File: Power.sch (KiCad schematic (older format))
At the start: 20 parts, among them U11 MCP1825S, U12 MP2456GJ-Z, U13 TLV75533PDBV

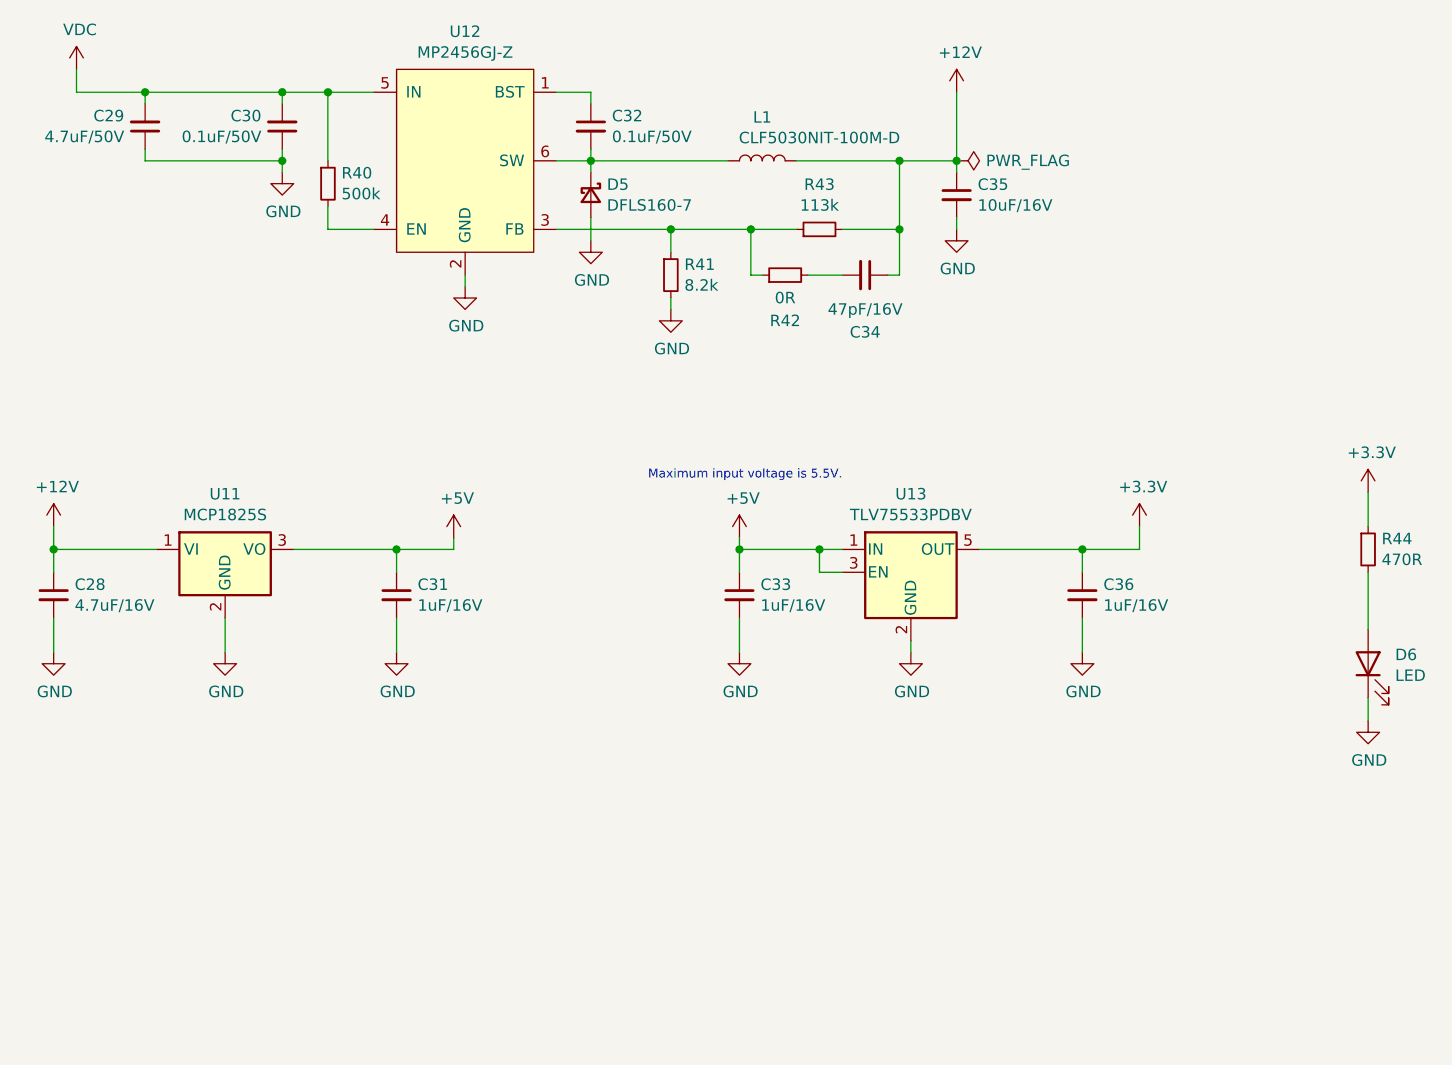
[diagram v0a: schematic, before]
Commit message: Update: 回路図、DCリンクCap1つ削除、アノテーションリセット
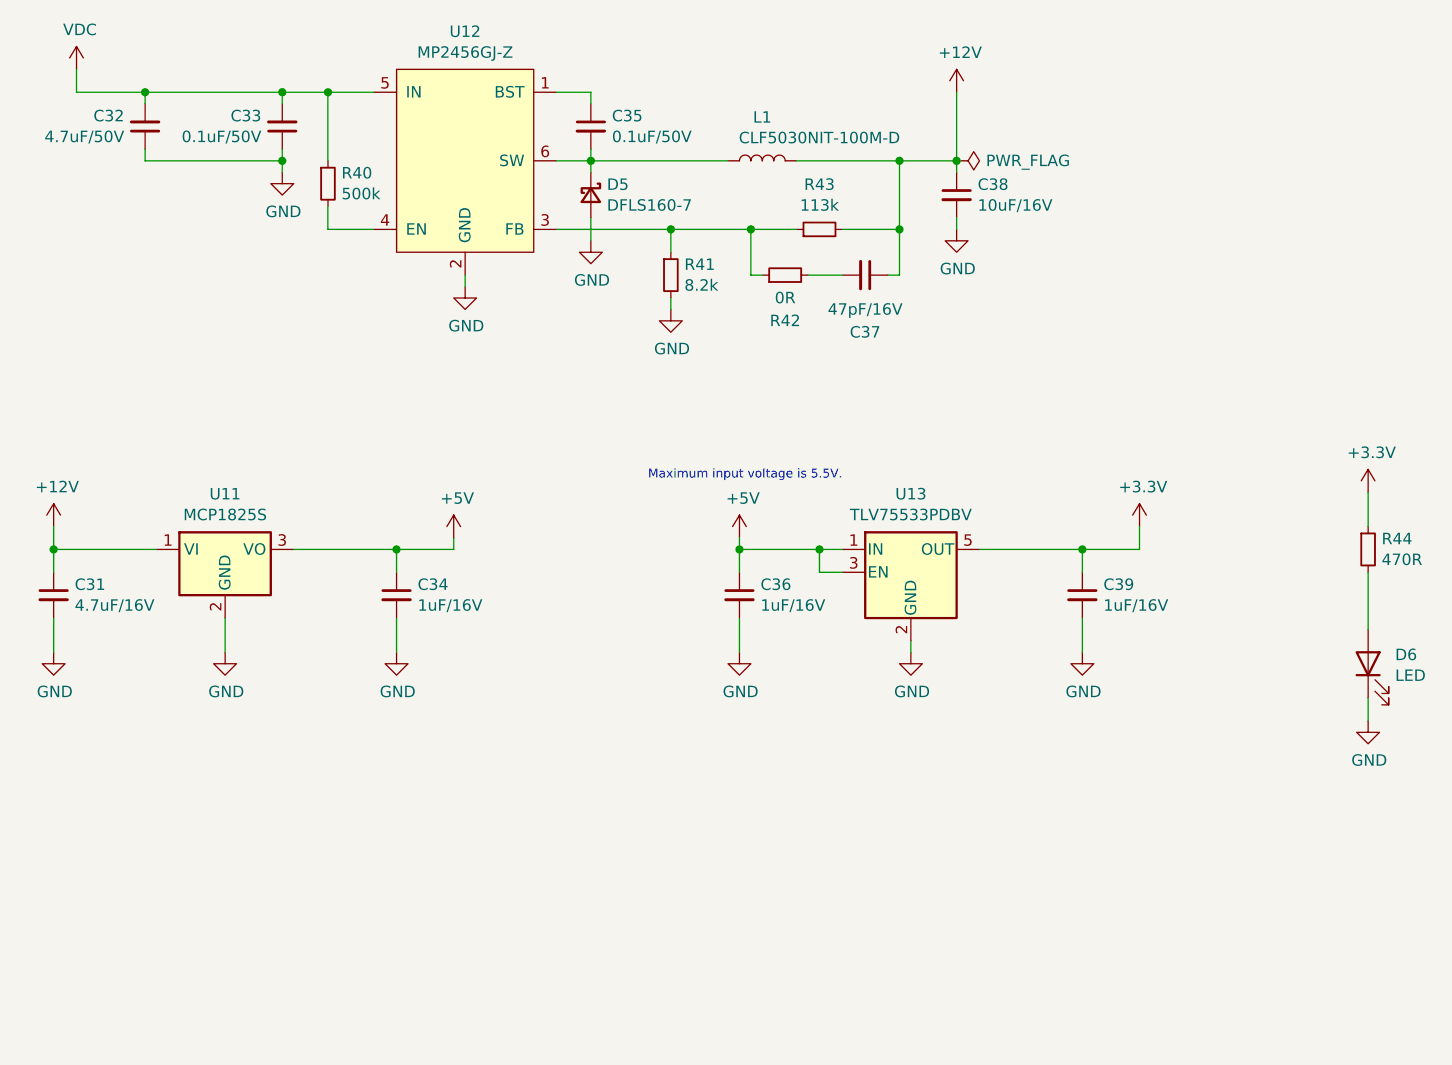
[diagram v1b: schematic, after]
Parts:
- renumbered C28 to C31, C29 to C32, C30 to C33, C31 to C34, C32 to C35, C33 to C36, C34 to C37, C35 to C38, C36 to C39
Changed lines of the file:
@@
 P 6700 1950
 AR Path="/60984E4D" Ref="C?"  Part="1"
-AR Path="/6093BF63/60984E4D" Ref="C35"  Part="1"
-F 0 "C35" H 6792 1996 50  0000 L CNN
+AR Path="/6093BF63/60984E4D" Ref="C38"  Part="1"
+F 0 "C38" H 6792 1996 50  0000 L CNN
 F 1 "10uF/16V" H 6792 1905 50  0000 L CNN
 F 2 "Capacitor_SMD:C_0805_2012Metric" H 6700 1950 50  0001 C CNN
@@
 P 5100 1650
 AR Path="/60984E53" Ref="C?"  Part="1"
-AR Path="/6093BF63/60984E53" Ref="C32"  Part="1"
-F 0 "C32" H 5192 1696 50  0000 L CNN
+AR Path="/6093BF63/60984E53" Ref="C35"  Part="1"
+F 0 "C35" H 5192 1696 50  0000 L CNN
 F 1 "0.1uF/50V" H 5192 1605 50  0000 L CNN
 F 2 "Capacitor_SMD:C_0603_1608Metric" H 5100 1650 50  0001 C CNN
@@
 P 3750 1650
 AR Path="/60984E87" Ref="C?"  Part="1"
-AR Path="/6093BF63/60984E87" Ref="C30"  Part="1"
-F 0 "C30" H 3659 1604 50  0000 R CNN
+AR Path="/6093BF63/60984E87" Ref="C33"  Part="1"
+F 0 "C33" H 3659 1604 50  0000 R CNN
 F 1 "0.1uF/50V" H 3659 1695 50  0000 R CNN
 F 2 "Capacitor_SMD:C_0603_1608Metric" H 3750 1650 50  0001 C CNN
@@
 P 6300 2300
 AR Path="/60984EA5" Ref="C?"  Part="1"
-AR Path="/6093BF63/60984EA5" Ref="C34"  Part="1"
-F 0 "C34" V 6550 2300 50  0000 C CNN
+AR Path="/6093BF63/60984EA5" Ref="C37"  Part="1"
+F 0 "C37" V 6550 2300 50  0000 C CNN
 F 1 "47pF/16V" V 6450 2300 50  0000 C CNN
 F 2 "Capacitor_SMD:C_0603_1608Metric" H 6300 2300 50  0001 C CNN
@@
 P 3150 1650
 AR Path="/60984EB3" Ref="C?"  Part="1"
-AR Path="/6093BF63/60984EB3" Ref="C29"  Part="1"
-F 0 "C29" H 3059 1604 50  0000 R CNN
+AR Path="/6093BF63/60984EB3" Ref="C32"  Part="1"
+F 0 "C32" H 3059 1604 50  0000 R CNN
 F 1 "4.7uF/50V" H 3059 1695 50  0000 R CNN
 F 2 "Capacitor_SMD:C_0805_2012Metric" H 3150 1650 50  0001 C CNN
@@
 P 2750 3700
 AR Path="/633C9961" Ref="C?"  Part="1"
-AR Path="/6093BF63/633C9961" Ref="C28"  Part="1"
-F 0 "C28" H 2842 3746 50  0000 L CNN
+AR Path="/6093BF63/633C9961" Ref="C31"  Part="1"
+F 0 "C31" H 2842 3746 50  0000 L CNN
 F 1 "4.7uF/16V" H 2842 3655 50  0000 L CNN
 F 2 "Capacitor_SMD:C_0805_2012Metric" H 2750 3700 50  0001 C CNN
@@
 P 4250 3700
 AR Path="/633D1C47" Ref="C?"  Part="1"
-AR Path="/6093BF63/633D1C47" Ref="C31"  Part="1"
-F 0 "C31" H 4342 3746 50  0000 L CNN
+AR Path="/6093BF63/633D1C47" Ref="C34"  Part="1"
+F 0 "C34" H 4342 3746 50  0000 L CNN
 F 1 "1uF/16V" H 4342 3655 50  0000 L CNN
 F 2 "Capacitor_SMD:C_0603_1608Metric" H 4250 3700 50  0001 C CNN
@@
 P 5750 3700
 AR Path="/633EC030" Ref="C?"  Part="1"
-AR Path="/6093BF63/633EC030" Ref="C33"  Part="1"
-F 0 "C33" H 5842 3746 50  0000 L CNN
+AR Path="/6093BF63/633EC030" Ref="C36"  Part="1"
+F 0 "C36" H 5842 3746 50  0000 L CNN
 F 1 "1uF/16V" H 5842 3655 50  0000 L CNN
 F 2 "Capacitor_SMD:C_0603_1608Metric" H 5750 3700 50  0001 C CNN
@@
 P 7250 3700
 AR Path="/633F2B77" Ref="C?"  Part="1"
-AR Path="/6093BF63/633F2B77" Ref="C36"  Part="1"
-F 0 "C36" H 7342 3746 50  0000 L CNN
+AR Path="/6093BF63/633F2B77" Ref="C39"  Part="1"
+F 0 "C39" H 7342 3746 50  0000 L CNN
 F 1 "1uF/16V" H 7342 3655 50  0000 L CNN
 F 2 "Capacitor_SMD:C_0603_1608Metric" H 7250 3700 50  0001 C CNN
@@
 	8500 4250 8500 4150
 $Comp
-L power:PWR_FLAG #FLG0106
+L power:PWR_FLAG #FLG06
 U 1 1 63927B2B
 P 6700 1800
-F 0 "#FLG0106" H 6700 1875 50  0001 C CNN
+F 0 "#FLG06" H 6700 1875 50  0001 C CNN
 F 1 "PWR_FLAG" V 6700 1928 50  0000 L CNN
 F 2 "" H 6700 1800 50  0001 C CNN

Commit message: Update: アナログリファレンスをLDOからに変更
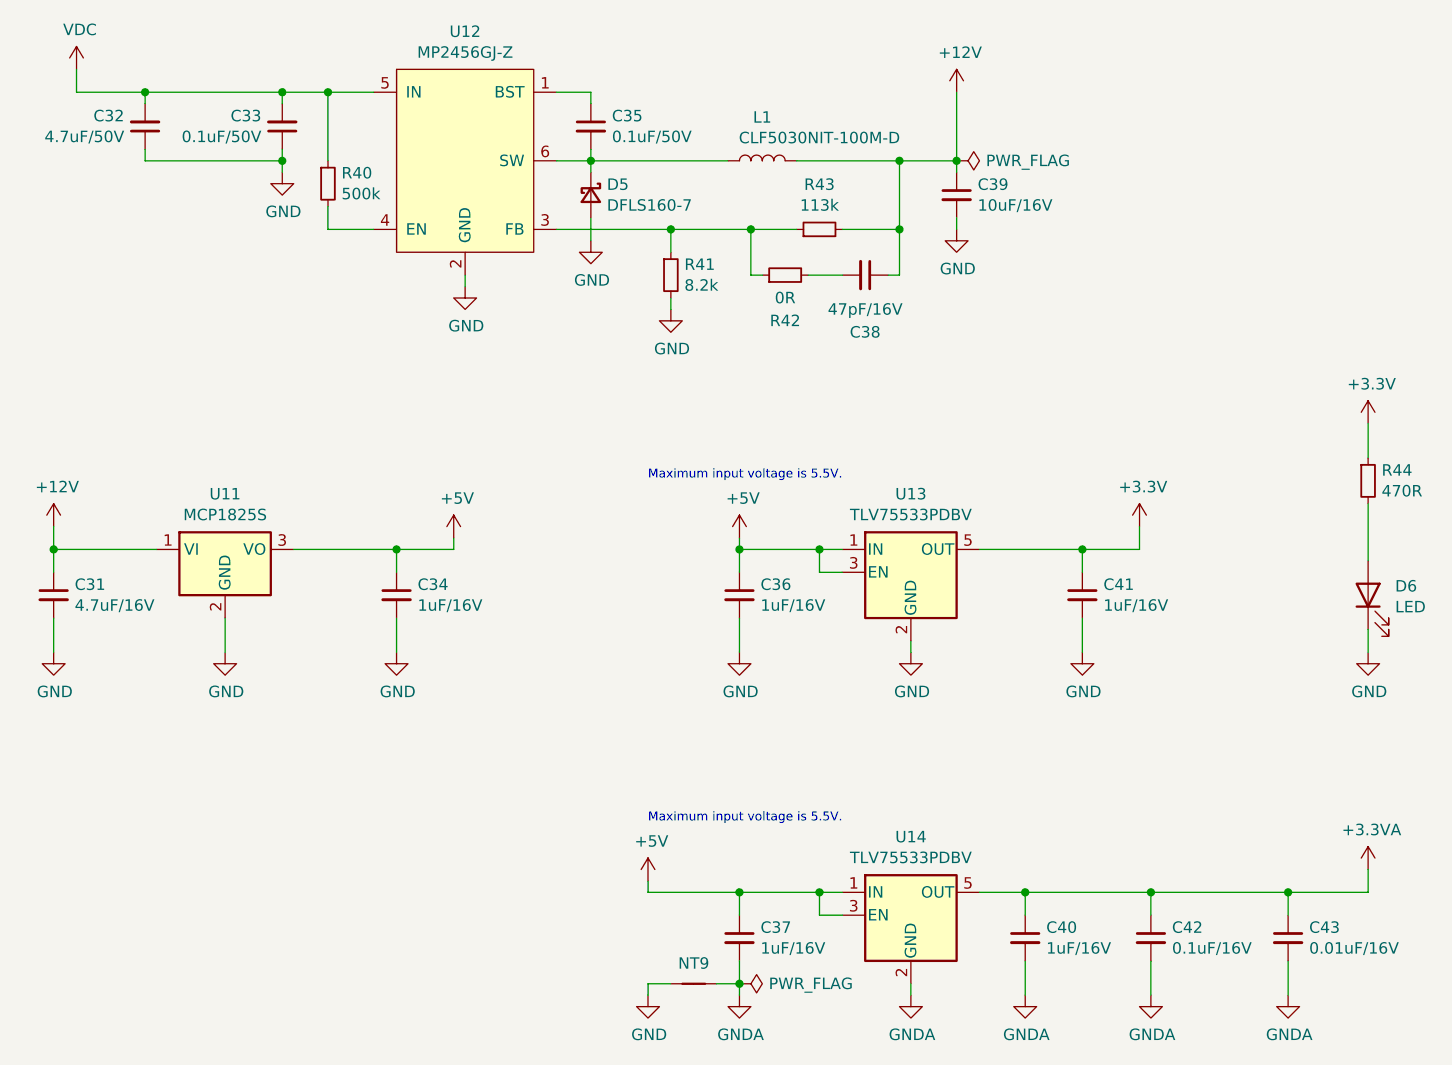
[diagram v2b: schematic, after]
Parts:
- added C37, C40: 1uF/16V, Capacitor_SMD:C_0603_1608Metric, symbol Device:C_Small
- added C42: 0.1uF/16V, Capacitor_SMD:C_0603_1608Metric, symbol Device:C_Small
- added C43: 0.01uF/16V, Capacitor_SMD:C_0603_1608Metric, symbol Device:C_Small
- added NT9: Net-Tie_2, NetTie:NetTie-2_SMD_Pad0.5mm, symbol Device:Net-Tie_2
- added U14: TLV75533PDBV, Package_TO_SOT_SMD:SOT-23-5, symbol Regulator_Linear:TLV75533PDBV
- renumbered C37 to C38, C38 to C39, C39 to C41
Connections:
- net +5V: now also C37.1, U14.1 (IN), U14.3 (EN)
- net GND: now also NT9.2
- new net +3.3VA: C40.1, C42.1, C43.1, U14.5 (OUT)
- new net GNDA: C37.2, C40.2, C42.2, C43.2, NT9.1, U14.2 (GND)
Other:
- moved on the sheet: D6, R44
